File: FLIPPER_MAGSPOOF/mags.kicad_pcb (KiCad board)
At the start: 2 copper layers, 67 x 23.3 mm, 23 parts, among them J1 Coil, J2 Conn_01x10_Socket, J3 Conn_01x08_Socket, U1 TC4424, U2 AP3602AKTR-G1

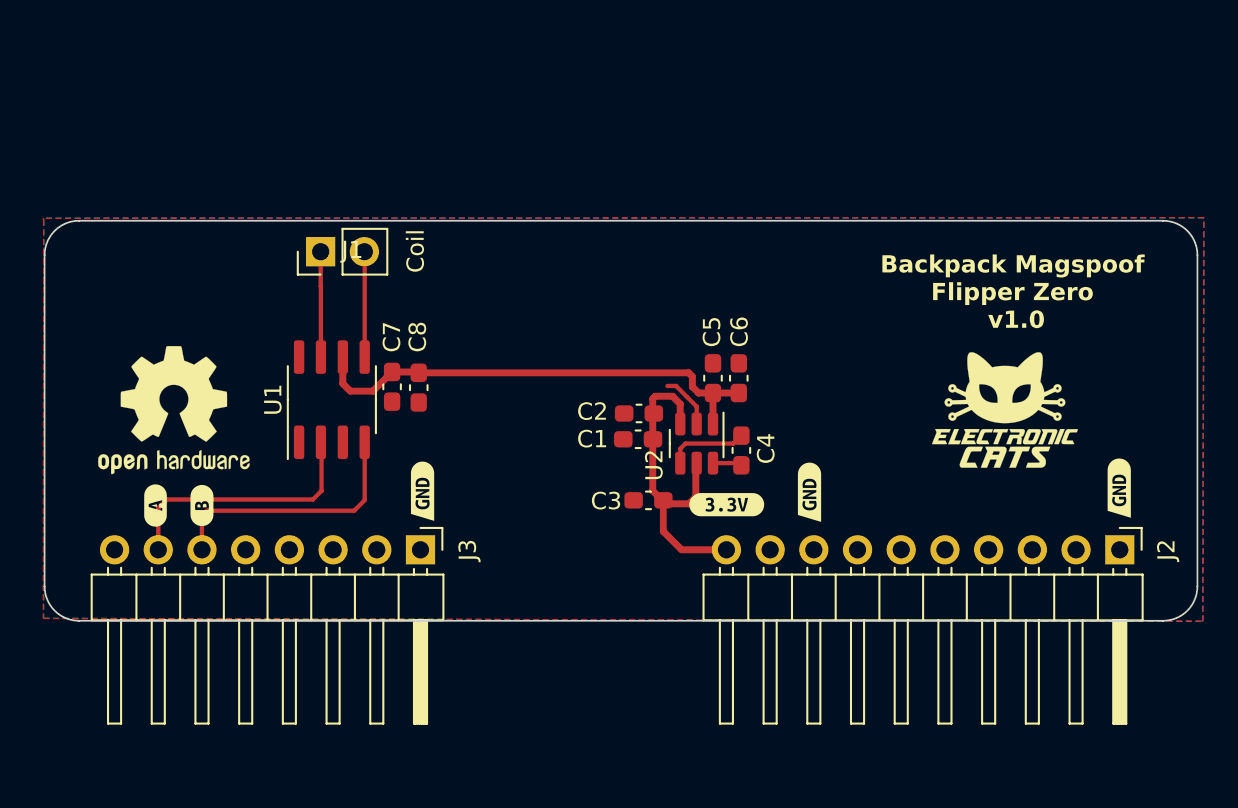
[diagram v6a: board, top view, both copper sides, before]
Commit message: Add_Pins_Remove_Boost
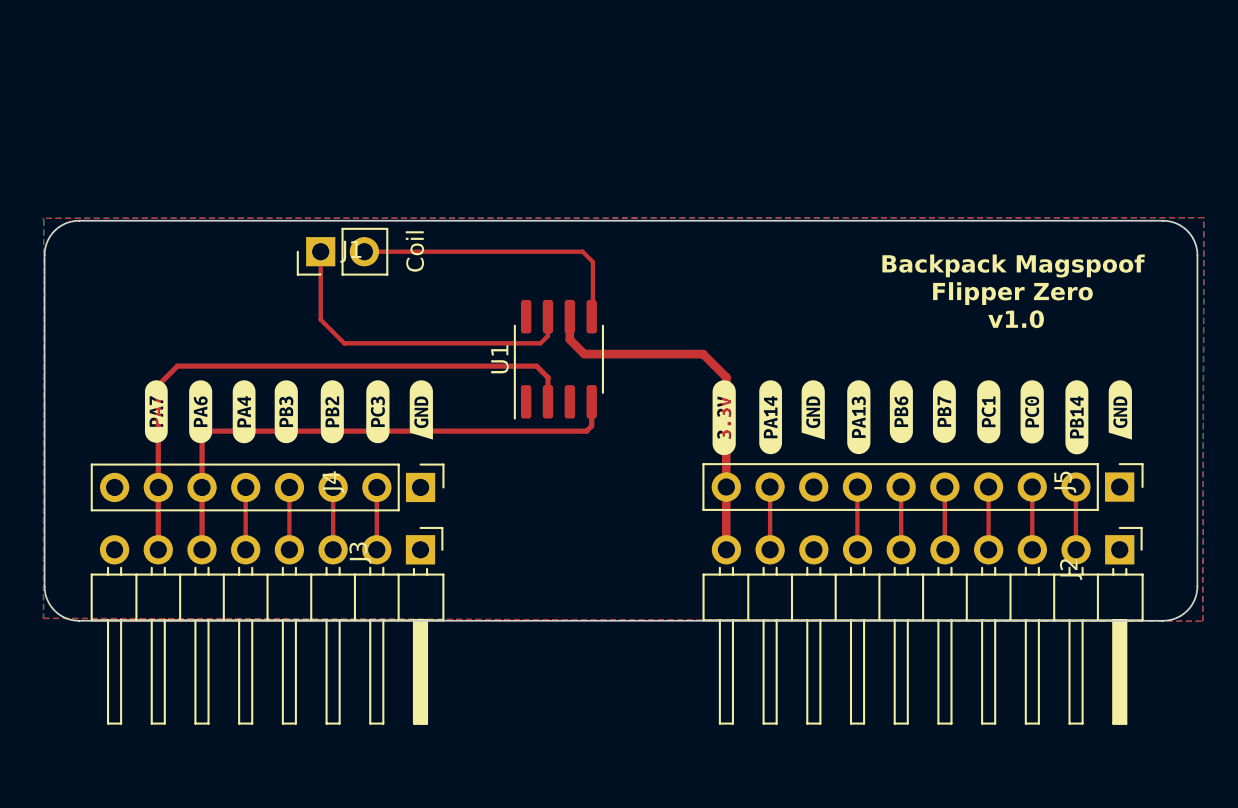
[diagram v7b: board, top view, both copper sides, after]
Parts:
- removed C1, C6, C8: 0.1uf, Capacitor_SMD:C_0603_1608Metric_Pad1.08x0.95mm_HandSolder
- removed C2, C3, C5, C7: 10uf, Capacitor_SMD:C_0603_1608Metric_Pad1.08x0.95mm_HandSolder
- removed C4: 1uf, Capacitor_SMD:C_0603_1608Metric_Pad1.08x0.95mm_HandSolder
- removed the G*** at (251.8, 74.4) (x2)
- removed the REF** at (203.5, 74.4) (x2)
- removed U2: AP3602AKTR-G1, Package_TO_SOT_SMD:TSOT-23-6
- removed kibuzzard-6488F7DC: G***, kibuzzard-6488F7DC
- removed kibuzzard-6488F7EB: G***, kibuzzard-6488F7EB
- added G***: LOGO, Aesthetics:electronic_cats_logo_4x3, B.Cu at (254.0, 67.5)
- added J4: Conn_01x08_Socket, Connector_PinHeader_2.54mm:PinHeader_1x08_P2.54mm_Vertical, F.Cu at (217.9, 78.9)
- added J5: Conn_01x10_Socket, Connector_PinHeader_2.54mm:PinHeader_1x10_P2.54mm_Vertical, F.Cu at (258.5, 78.9)
- added REF**: OSHW-Logo_11.4x12mm_SilkScreen, Symbol:OSHW-Logo_11.4x12mm_SilkScreen, B.Cu at (203.1, 69.2)
- added kibuzzard-648B91CB: G***, kibuzzard-648B91CB, F.Cu at (207.6, 74.5)
- added kibuzzard-648B91E6: G***, kibuzzard-648B91E6, F.Cu at (210.1, 74.5)
- added kibuzzard-648B91FC: G***, kibuzzard-648B91FC, F.Cu at (212.7, 74.5)
- added kibuzzard-648B921B: G***, kibuzzard-648B921B, F.Cu at (215.4, 74.5)
- added kibuzzard-648B922F: G***, kibuzzard-648B922F, F.Cu at (202.5, 74.5)
- added kibuzzard-648B923F: G***, kibuzzard-648B923F, F.Cu at (205.1, 74.5)
- added kibuzzard-648B93B1: G***, kibuzzard-648B93B1, F.Cu at (238.2, 74.8)
- added kibuzzard-648B93BF: G***, kibuzzard-648B93BF, F.Cu at (243.3, 74.8)
- added kibuzzard-648B93D2: G***, kibuzzard-648B93D2, F.Cu at (248.3, 74.5)
- added kibuzzard-648B93E0: G***, kibuzzard-648B93E0, F.Cu at (245.8, 74.5)
- added kibuzzard-648B93EF: G***, kibuzzard-648B93EF, F.Cu at (250.9, 74.5)
- added kibuzzard-648B9401: G***, kibuzzard-648B9401, F.Cu at (253.4, 74.5)
- added kibuzzard-648B9410: G***, kibuzzard-648B9410, F.Cu at (256.0, 74.8)
- moved U1 13.4 mm to (225.9, 71.5)
- moved kibuzzard-6488F75A 5.05 mm to (235.5, 74.8), turned to 90 degrees
- moved kibuzzard-6488EEAF 4.79 mm to (240.7, 74.4)
- moved kibuzzard-6488EEAF 4.72 mm to (217.9, 74.4)
- moved kibuzzard-6488EEAF 4.54 mm to (258.5, 74.4)
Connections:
- J2 pad 2: unconnected-(J2-Pin_9-Pad2) -> /PB14
- J2 pad 3: unconnected-(J2-Pin_8-Pad3) -> /PC0
- J2 pad 4: unconnected-(J2-Pin_7-Pad4) -> /PC1
- J2 pad 5: unconnected-(J2-Pin_6-Pad5) -> /PB7
- J2 pad 6: unconnected-(J2-Pin_5-Pad6) -> /PB6
- J2 pad 7: unconnected-(J2-Pin_4-Pad7) -> /PA13
- J2 pad 9: unconnected-(J2-Pin_2-Pad9) -> /PA14
- J3 pad 2: unconnected-(J3-Pin_7-Pad2) -> /PC3
- J3 pad 3: unconnected-(J3-Pin_6-Pad3) -> /PB2
- J3 pad 4: unconnected-(J3-Pin_5-Pad4) -> /PB3
- J3 pad 5: unconnected-(J3-Pin_4-Pad5) -> /PA4
- U1 pad 6: +5V -> +3V3
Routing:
- net +5V: track 27.9 -> 0.00 mm
- net /IN_A: track 14.9 -> 34.4 mm
- net /IN_B: track 15.2 -> 30.8 mm
- net /Out_A: track 6.13 -> 19.0 mm
- net /Out_B: track 6.13 -> 16.7 mm
- net Net-(U2-C-): track 4.70 -> 0.00 mm
- net /PC1: track 0.00 -> 3.65 mm
- net /PC0: track 0.00 -> 3.65 mm
- net /PB7: track 0.00 -> 3.65 mm
- net /PB6: track 0.00 -> 3.65 mm
- net /PB14: track 0.00 -> 3.65 mm
- net /PA14: track 0.00 -> 3.65 mm
- net /PA13: track 0.00 -> 3.65 mm
- net /PC3: track 0.00 -> 3.64 mm
- net /PB3: track 0.00 -> 3.62 mm
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
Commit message: Move_Pins
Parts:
- moved J1 6.93 mm to (211.5, 58.3)
- moved kibuzzard-6488EEAF 3.21 mm to (217.7, 77.6)
- moved kibuzzard-648B91CB 3.21 mm to (207.4, 77.7)
- moved kibuzzard-648B91E6 3.21 mm to (209.8, 77.7)
- moved kibuzzard-648B91FC 3.21 mm to (212.5, 77.7)
- moved kibuzzard-648B921B 3.21 mm to (215.2, 77.7)
- moved kibuzzard-648B922F 3.21 mm to (202.3, 77.7)
- moved kibuzzard-648B923F 3.21 mm to (204.9, 77.7)
- moved kibuzzard-6488EEAF 2.82 mm to (240.6, 77.2)
- moved kibuzzard-6488F75A 2.82 mm to (235.4, 77.7)
- moved kibuzzard-648B93D2 2.82 mm to (248.2, 77.3)
- moved kibuzzard-648B93E0 2.82 mm to (245.7, 77.3)
- moved kibuzzard-648B93EF 2.82 mm to (250.8, 77.3)
- moved kibuzzard-648B9401 2.82 mm to (253.3, 77.3)
- moved kibuzzard-648B9410 2.82 mm to (255.9, 77.6)
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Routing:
- net /Out_A: track 19.0 -> 26.2 mm
- net /Out_B: track 16.7 -> 23.4 mm
- net +3V3: track 21.4 -> 24.2 mm
- net /PC3: track 3.64 -> 6.26 mm
- net /IN_B: track 30.8 -> 33.4 mm
- net /IN_A: track 34.4 -> 36.9 mm
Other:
- board size 67 x 23.3 mm -> 66 x 30.5 mm
- rule pad_to_mask_clearance: 0 -> 0.051
